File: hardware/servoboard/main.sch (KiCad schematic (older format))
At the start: 42 parts, among them IC1 ATMEGA8-P, K1 CS1, K10 CPOW2, K11 I2C, K2 CS2, K3 CS3, K4 CS4, K5 CS5, K6 CS6, K7 CS7, K8 CS8, K9 CPOW, P1 PROG, P3 JSE, Q1 IRFZ24N, X1 12MHz

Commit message: servoboard - 7805 integration
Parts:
- removed Q1: IRFZ24N, symbol MOS_N
- added C15, C16, C17, C18: 100nF, symbol C
- added K12: JPSel, symbol CONN_3
- added K13: I2CBIG, symbol CONN_3
- added Q1: IRFZ24N, ~, symbol MOS_N_CORRECT_PINS
- added U1: 7805_CORRECT_PINS, ~, symbol 7805_CORRECT_PINS
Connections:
- net labels added: VLogicIn, VToReg
- wire segments 130 -> 147
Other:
- moved on the sheet: D5, K11, R5, R6, R7

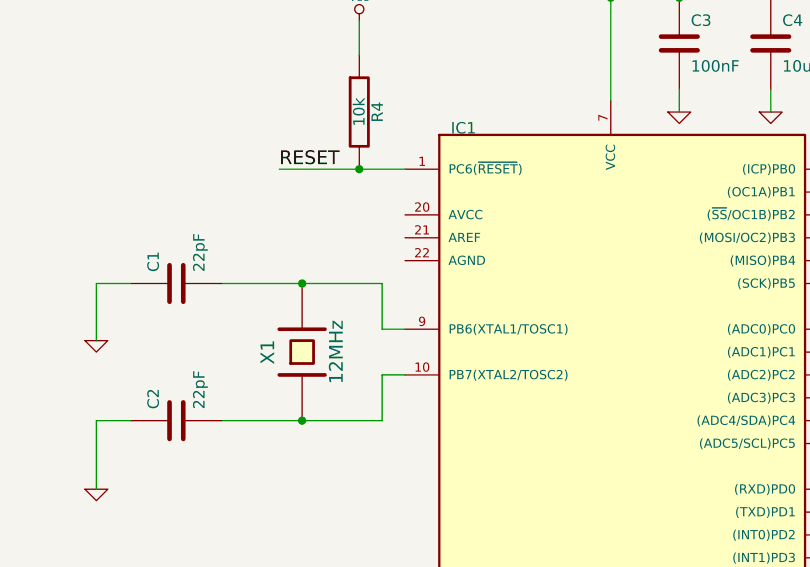
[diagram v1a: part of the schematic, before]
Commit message: servoboard firmware: twi protocol
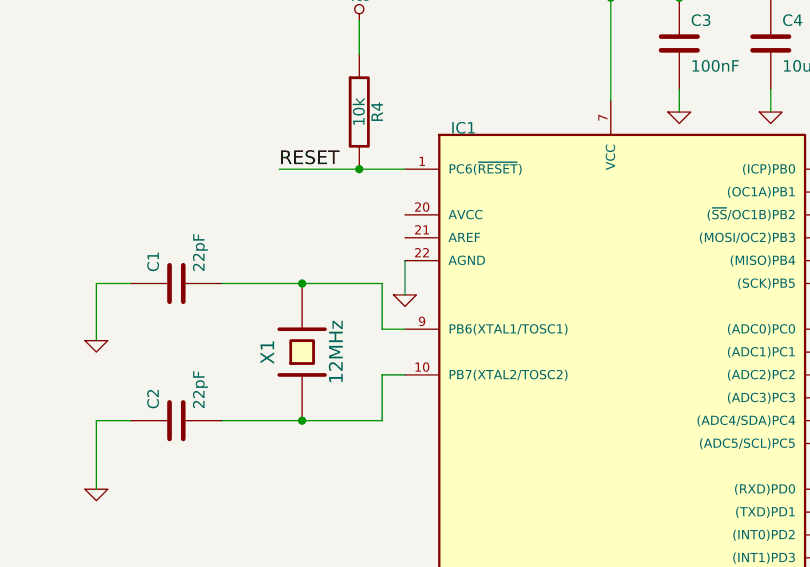
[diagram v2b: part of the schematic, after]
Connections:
- wire segments 147 -> 148
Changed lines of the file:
@@
-EESchema Schematic File Version 2  date Tue 07 May 2013 01:08:31 PM CEST
+EESchema Schematic File Version 2  date Tue 07 May 2013 11:36:32 PM CEST
 LIBS:power
 LIBS:device
@@
 	9400 3000 9500 3000
 Connection ~ 9200 3500
+$Comp
+L GND #PWR?
+U 1 1 51897642
+P 2750 3050
+F 0 "#PWR?" H 2750 3050 30  0001 C CNN
+F 1 "GND" H 2750 2980 30  0001 C CNN
+F 2 "" H 2750 3050 60  0001 C CNN
+F 3 "" H 2750 3050 60  0001 C CNN
+	1    2750 3050
+	1    0    0    -1
+$EndComp
+Wire Wire Line
+	2750 3050 2750 2900
 $EndSCHEMATC
